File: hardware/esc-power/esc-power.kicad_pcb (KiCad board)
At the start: 2 copper layers, 50 x 50 mm, 9 parts, among them P1 CONN_01X02, P2 CONN_01X02, P3 CONN_01X02, P4 CONN_01X02, P5 CONN_01X02, P6 CONN_01X02, P7 CONN_01X02, P8 CONN_01X02, P9 CONN_01X02

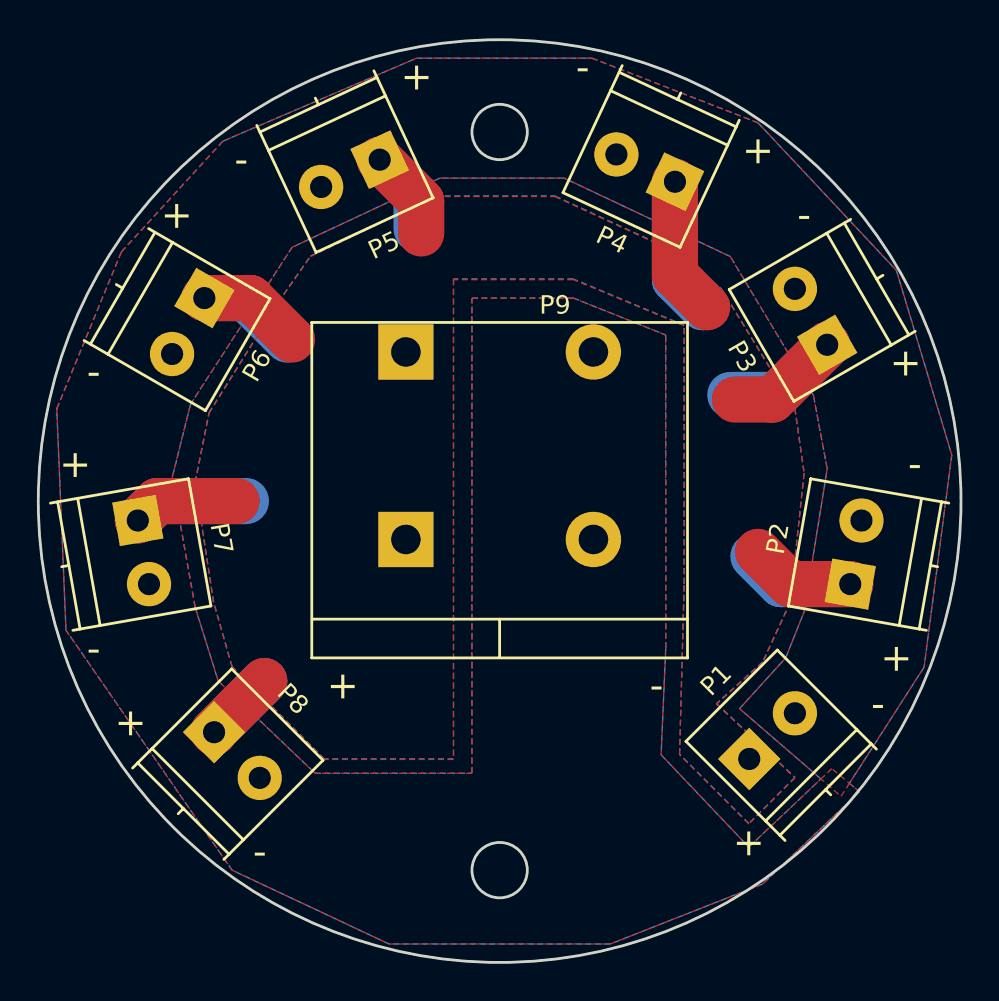
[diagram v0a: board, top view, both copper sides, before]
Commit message: Using components with 5mm pitch
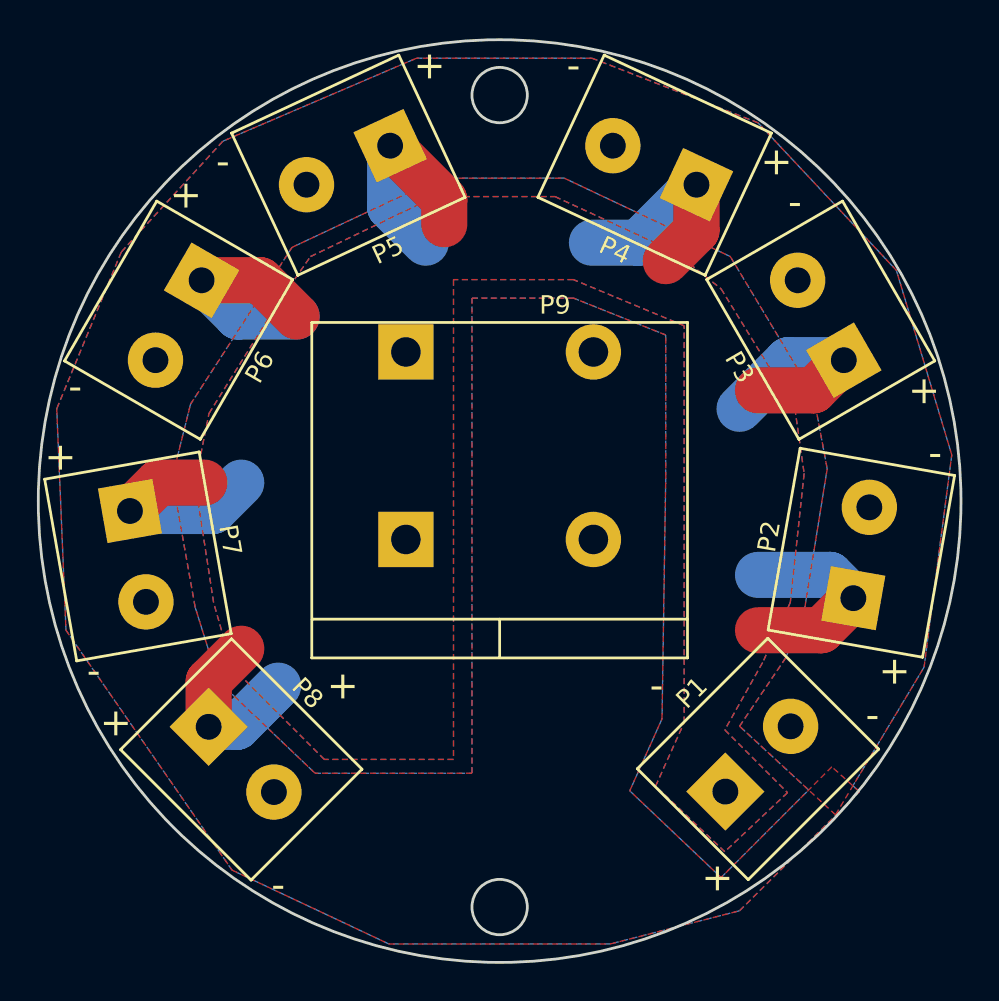
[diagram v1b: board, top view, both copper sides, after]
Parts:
- P1, P2, P3, P4, P5, P6, P7, P8: footprint Terminal_Blocks:TerminalBlock_Pheonix_PT-3.5mm_2pol -> Sigmadrone:WURTH_691131710002
- moved P8 2.09 mm to (96.0, 84.0)
- moved P7 1.95 mm to (90.4, 73.0)
- moved P6 1.84 mm to (92.6, 60.2)
- moved P2 1.80 mm to (129.6, 72.8)
- moved P5 1.73 mm to (101.8, 51.8)
- moved P4 1.42 mm to (118.4, 51.8)
- moved P3 1.38 mm to (127.4, 60.2)
- moved P1 0.47 mm to (124.0, 84.0)
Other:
- outline, holes or cut-outs redrawn

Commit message: Modified the project settings
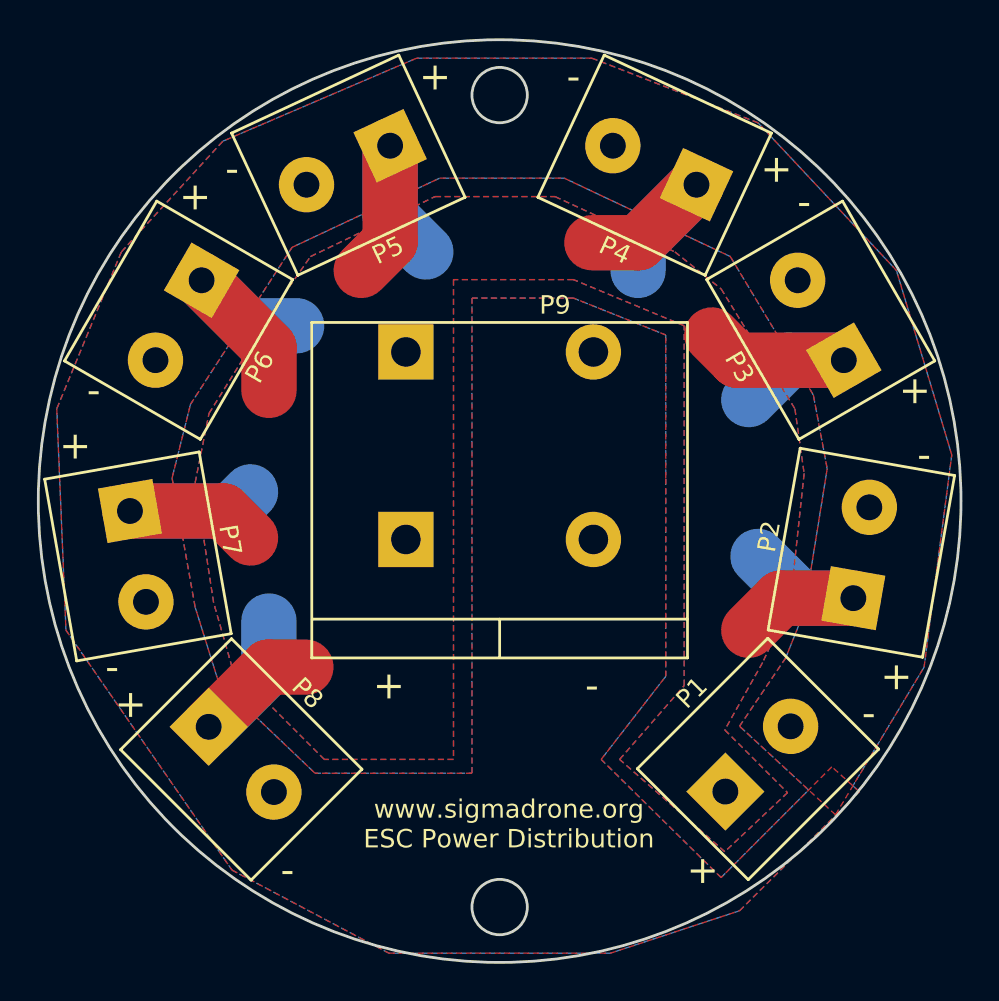
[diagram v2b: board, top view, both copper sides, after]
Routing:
- net +BATT: track 79.9 -> 94.6 mm
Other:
- board text added: "www.sigmadrone.org ESC Power Distribution"
